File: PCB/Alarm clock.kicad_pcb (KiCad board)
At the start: 2 copper layers, 4 parts, among them J1 TFT, J2 Conn_01x06_Female, SW1 SW_MEC_5G, U1 ESP32-C3_SUPERMINI

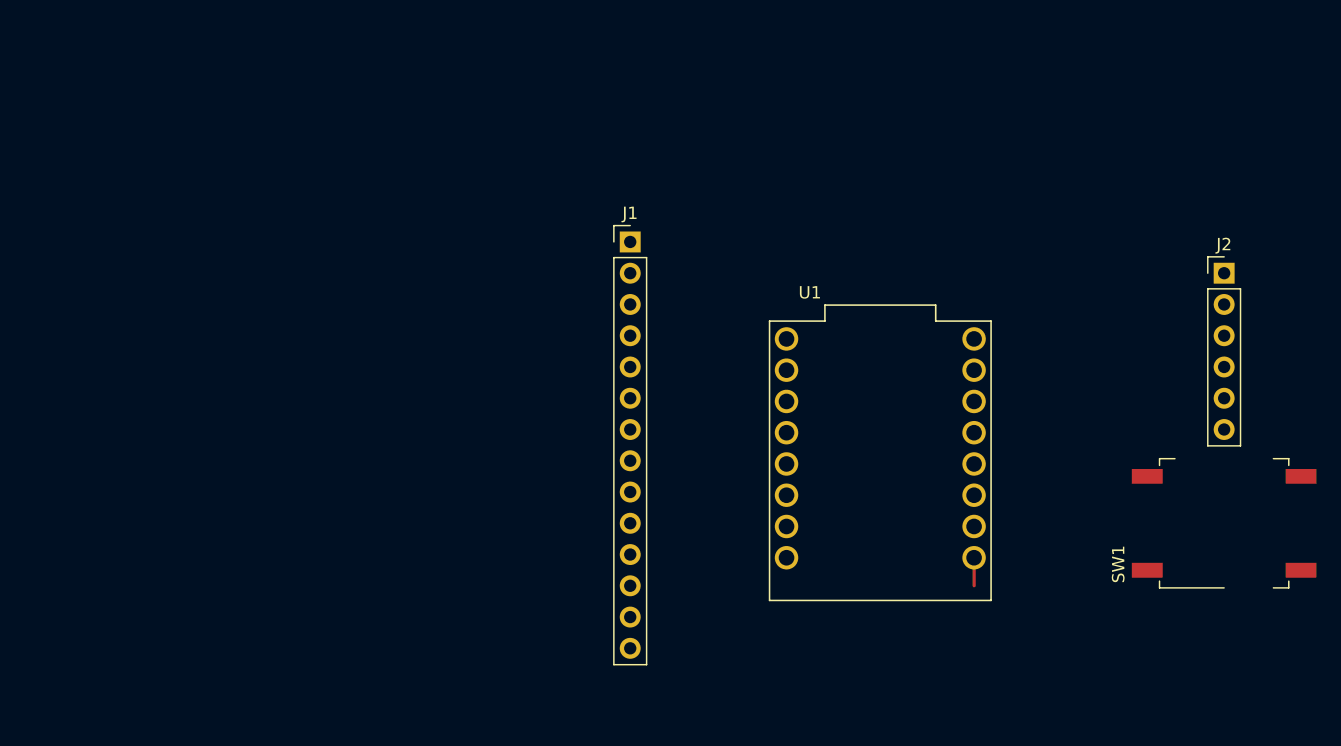
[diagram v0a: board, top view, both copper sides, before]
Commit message: Use Hardware SPI and start working on SD support
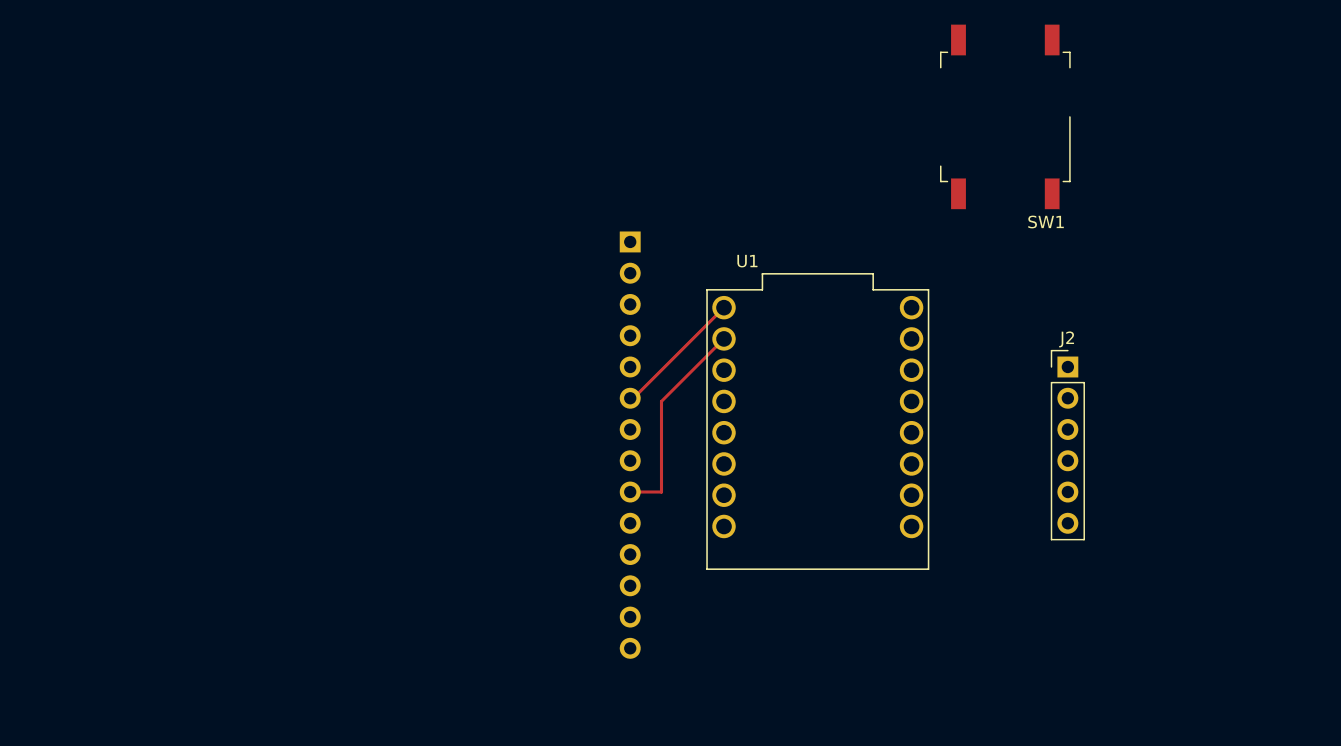
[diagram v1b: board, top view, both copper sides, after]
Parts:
- J1: moved to B.Cu
- J2: value Conn_01x06_Female -> RTC
- moved SW1 37.5 mm to (167.6, 61.0), turned to 180 degrees
- moved J2 14.8 mm to (172.7, 81.3)
- moved U1 5.68 mm to (152.4, 86.4)
- turned J1 to 180 degrees
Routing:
- net Net-(J1-Pad9): track 0.00 -> 17.1 mm
- net Net-(J1-Pad6): track 0.00 -> 10.7 mm
- net unconnected-(U1-Pad0): track 2.28 -> 0.00 mm
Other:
- copper layers 2 -> 4

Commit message: PCB Update
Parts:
- SW1: value SW_MEC_5G -> SW_Push; footprint Button_Switch_SMD:SW_MEC_5GSH9 -> Button_Switch_THT:SW_PUSH_6mm; moved to B.Cu
- moved J1 46.1 mm to (91.4, 65.0)
- moved U1 41.0 mm to (111.8, 81.3)
- moved J2 31.0 mm to (147.3, 63.5), turned to 90 degrees
- moved SW1 28.1 mm to (182.9, 84.5), turned to 90 degrees
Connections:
- SW1 pad 1: Net-(SW1-Pad1) -> Net-(U1-Pad10)
- SW1 pad 2: Net-(SW1-Pad1) -> GND
- U1 pad 10: Net-(SW1-Pad1) -> Net-(U1-Pad10)
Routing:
- net +5V: track 0.00 -> 61.4 mm, vias 0 -> 1
- net Net-(J1-Pad8): track 0.00 -> 37.1 mm, vias 0 -> 1
- net Net-(J1-Pad12): track 0.00 -> 32.1 mm
- net Net-(J1-Pad11): track 0.00 -> 22.5 mm
- net Net-(J1-Pad10): track 0.00 -> 10.7 mm
- net Net-(J1-Pad9): track 17.1 -> 20.9 mm
- net GND: track 0.00 -> 2.80 mm, vias 0 -> 1
- net Net-(J1-Pad6): track 10.7 -> 12.8 mm
- added copper zone on B.Cu, net GND
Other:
- board outline added: 98 x 55 mm
